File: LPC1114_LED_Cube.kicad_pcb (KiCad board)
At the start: 2 copper layers, 100 x 100 mm, 66 parts, among them Q201 BSS138, Q202 BSS138, Q203 BSS138, Q204 BSS138, Q205 IRLML6402TRPBF, Q206 IRLML6402TRPBF, Q207 IRLML6402TRPBF, Q208 IRLML6402TRPBF, Q209 BSS138, Q210 BSS138, Q211 BSS138, Q212 BSS138, Q213 IRLML6402TRPBF, Q214 IRLML6402TRPBF, Q215 IRLML6402TRPBF, Q216 IRLML6402TRPBF, Y101 12MHZ, Y102 12MHZ

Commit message: More pcb layout
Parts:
- moved LED/SPI_0 58.1 mm to (163.4, 83.1), turned to 0 degrees
- moved LED_CH0_CTRL0 0.50 mm to (92.7, 86.4)
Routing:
- net VPRG: track 0.00 -> 111.3 mm, vias 0 -> 5
- net XERR_CH0: track 0.00 -> 100.6 mm, vias 0 -> 4
- net DCPRG: track 0.00 -> 72.7 mm, vias 0 -> 4
- net ISP_ENTRY: track 0.00 -> 71.6 mm, vias 0 -> 4
- net XLAT: track 0.00 -> 61.8 mm, vias 0 -> 4
- net LED_DATA_SCK: track 0.00 -> 59.8 mm, vias 0 -> 4
- net BLANK: track 0.00 -> 59.6 mm, vias 0 -> 4
- net LED_CH2_8: track 0.00 -> 44.0 mm
- net LED_CH2_9: track 0.00 -> 40.4 mm
- net LED_CH3_0: track 0.00 -> 37.6 mm
- net LED_CH3_1: track 0.00 -> 37.3 mm, vias 0 -> 1
- net LED_CH3_2: track 0.00 -> 36.9 mm, vias 0 -> 1
- net LED_CH2_10: track 0.00 -> 36.7 mm
- net LED_CH3_3: track 0.00 -> 36.2 mm, vias 0 -> 1
- net LED_CH3_4: track 0.00 -> 34.5 mm, vias 0 -> 1
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
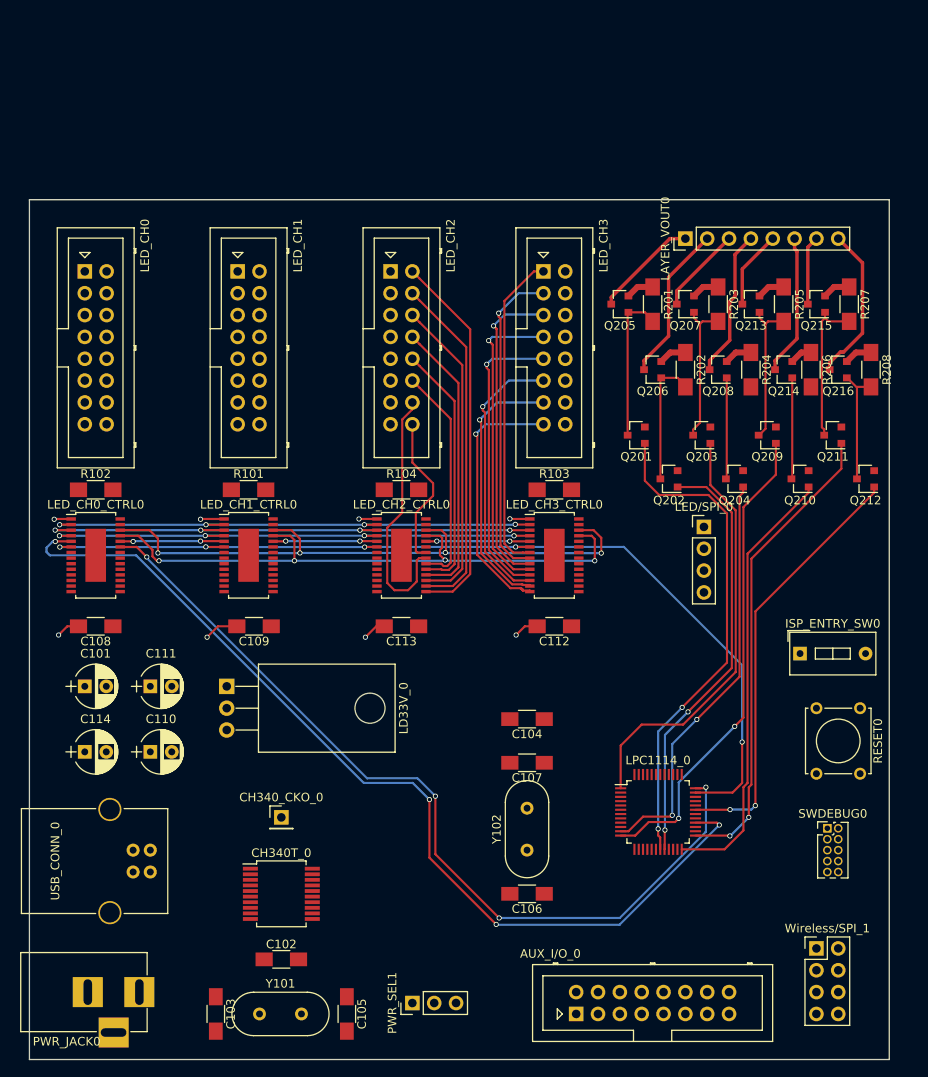
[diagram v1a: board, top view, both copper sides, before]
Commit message: redo layout for EMC
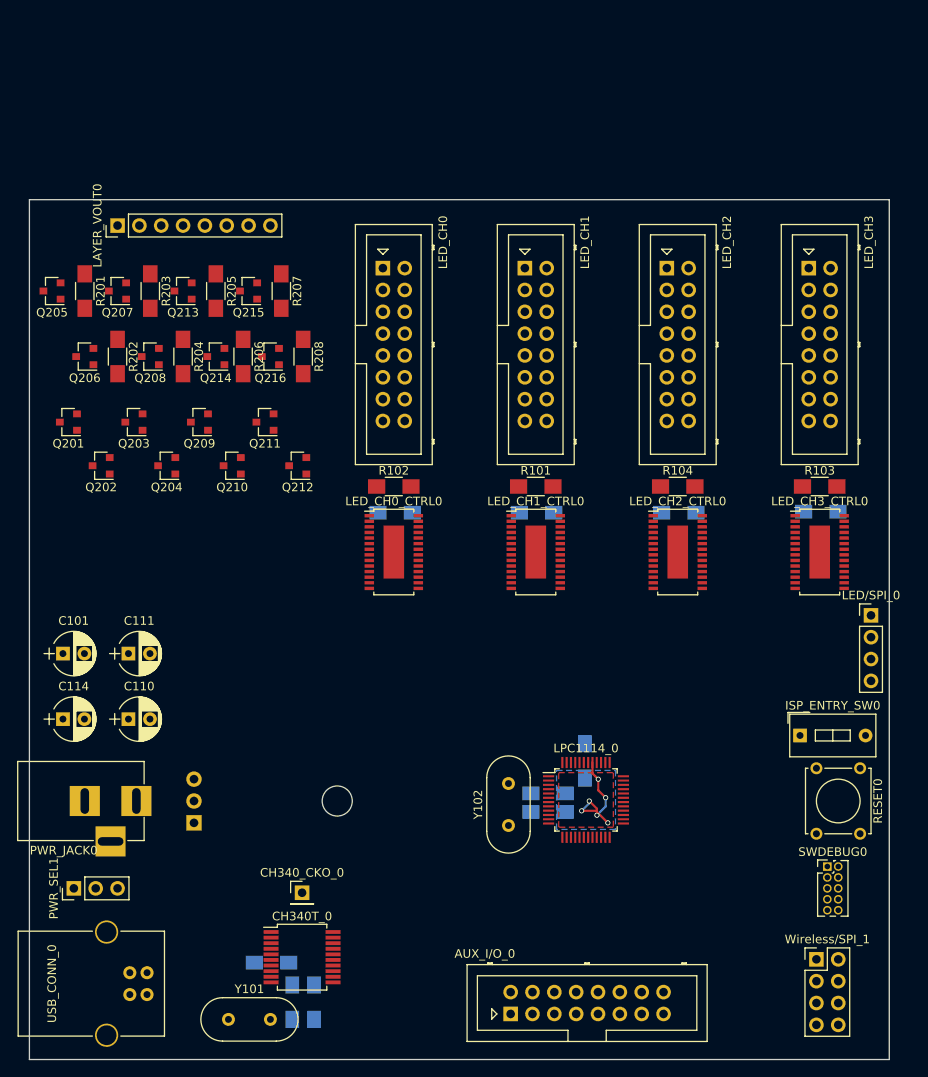
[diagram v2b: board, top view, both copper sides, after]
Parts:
- C102, C103, C104, C105, C106, C107, C108, C109, C112, C113, LD33V_0: moved to B.Cu
- moved Q210 66.1 mm to (108.6, 75.9)
- moved Q211 66.1 mm to (112.4, 70.9)
- moved Q212 66.1 mm to (116.2, 75.9)
- moved Q215 66.1 mm to (110.5, 55.6)
- moved R206 66.1 mm to (109.9, 63.2)
- moved R207 66.1 mm to (114.3, 55.6)
- moved LAYER_VOUT0 66.1 mm to (95.2, 48.0)
- moved Q201 66.1 mm to (89.5, 70.9)
- moved Q202 66.1 mm to (93.3, 75.9)
- moved Q203 66.1 mm to (97.2, 70.9)
- moved Q204 66.1 mm to (101.0, 75.9)
- moved Q205 66.1 mm to (87.6, 55.6)
- moved Q206 66.1 mm to (91.4, 63.2)
- moved Q207 66.1 mm to (95.2, 55.6)
- moved Q208 66.1 mm to (99.1, 63.2)
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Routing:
- net LED_SIN: track 111.5 -> 0.00 mm, vias 4 -> 0
- net VPRG: track 111.3 -> 0.00 mm, vias 5 -> 0
- net XERR_CH0: track 100.6 -> 0.00 mm, vias 4 -> 0
- net DCPRG: track 72.7 -> 0.00 mm, vias 4 -> 0
- net ISP_ENTRY: track 71.6 -> 0.00 mm, vias 4 -> 0
- net XLAT: track 61.8 -> 0.00 mm, vias 4 -> 0
- net LED_DATA_SCK: track 59.8 -> 0.00 mm, vias 4 -> 0
- net BLANK: track 59.6 -> 0.00 mm, vias 4 -> 0
- net LAYER_0_ON: track 57.9 -> 0.00 mm, vias 2 -> 0
- net LAYER_4_ON: track 55.9 -> 0.00 mm, vias 2 -> 0
- net LAYER_6_ON: track 55.1 -> 0.00 mm, vias 2 -> 0
- net LAYER_5_ON: track 51.2 -> 0.00 mm
- net LAYER_1_ON: track 49.9 -> 0.00 mm, vias 2 -> 0
- net LAYER_7_ON: track 49.9 -> 0.00 mm, vias 2 -> 0
- net LAYER_2_ON: track 49.7 -> 0.00 mm
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- added copper zone on B.Cu, net GND
- added copper zone on F.Cu, net GND
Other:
- rule trace_min: 0.2 -> 0.1524

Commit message: Fixed some schematic bugs. Added input mode switch.
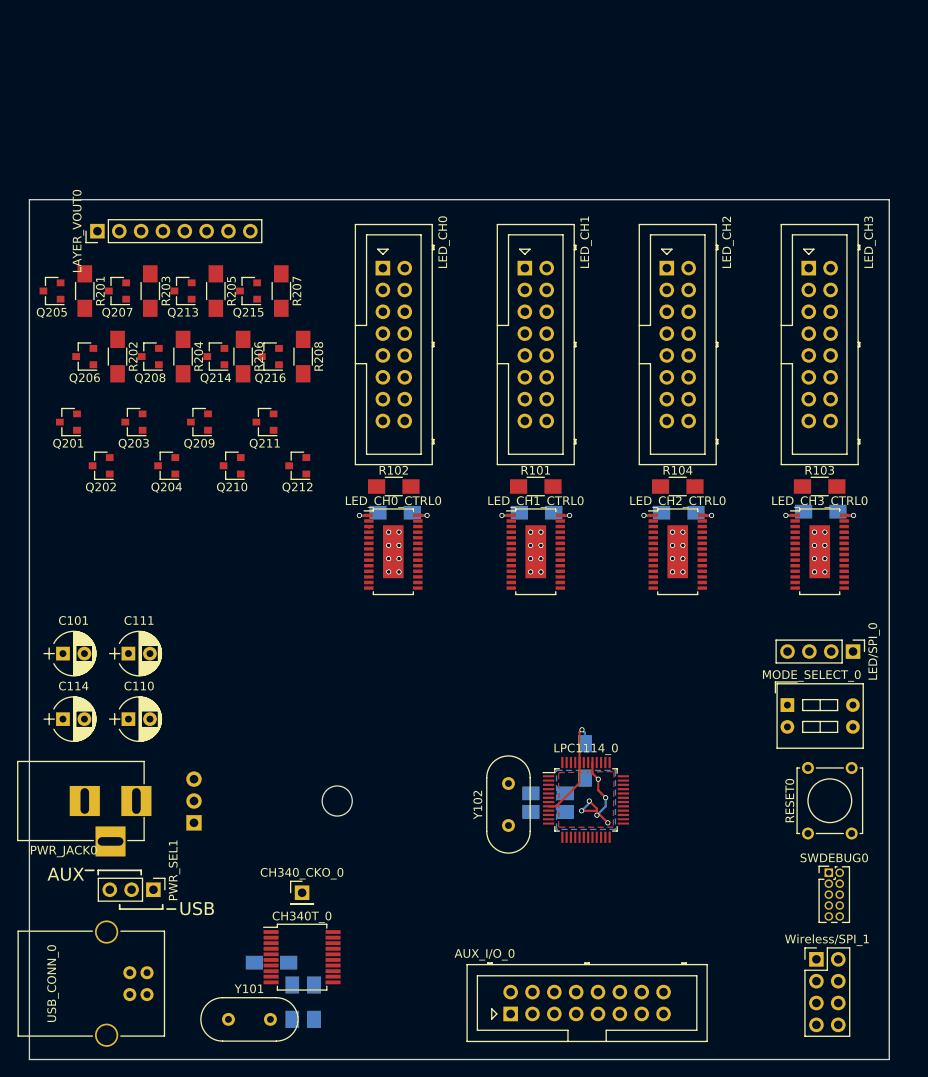
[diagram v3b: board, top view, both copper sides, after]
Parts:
- removed ISP_ENTRY_SW0: SW_DIP_x01, Buttons_Switches_THT:SW_DIP_x1_W7.62mm_Slide
- added MODE_SELECT_0: SW_DIP_x02, Buttons_Switches_THT:SW_DIP_x2_W7.62mm_Slide, F.Cu at (173.2, 103.8)
- moved RESET0 9.71 mm to (175.5, 118.7), turned to 90 degrees
- moved PWR_SEL1 9.26 mm to (99.4, 125.3), turned to 270 degrees
- moved LED/SPI_0 4.70 mm to (180.8, 97.6), turned to 270 degrees
- moved LAYER_VOUT0 2.43 mm to (92.9, 48.7)
- moved SWDEBUG0 0.75 mm to (178.0, 123.3)
- moved LED_CH0_CTRL0 0.07 mm to (127.3, 85.9)
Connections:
- net PIO0_2 renamed INPUT_MODE_SELECT
- C104 pad 1: +3V3 -> V3
- C108 pad 1: +3V3 -> V3
- C109 pad 1: +3V3 -> V3
- C112 pad 1: +3V3 -> V3
- C113 pad 1: +3V3 -> V3
- CH340T_0 pad 11: Net-(CH340T_0-Pad11) -> (no net)
- CH340T_0 pad 12: Net-(CH340T_0-Pad12) -> (no net)
- CH340T_0 pad 13: Net-(CH340T_0-Pad13) -> (no net)
- CH340T_0 pad 14: Net-(CH340T_0-Pad14) -> (no net)
- CH340T_0 pad 15: Net-(CH340T_0-Pad15) -> (no net)
- CH340T_0 pad 16: Net-(CH340T_0-Pad16) -> (no net)
- CH340T_0 pad 17: Net-(CH340T_0-Pad17) -> (no net)
- CH340T_0 pad 18: Net-(CH340T_0-Pad18) -> (no net)
- CH340T_0 pad 2: Net-(CH340T_0-Pad2) -> (no net)
- CH340T_0 pad 20: Net-(CH340T_0-Pad20) -> (no net)
- LED_CH0_CTRL0 pad 28: +3V3 -> V3
- LED_CH1_CTRL0 pad 28: +3V3 -> V3
- LED_CH2_CTRL0 pad 28: +3V3 -> V3
- LED_CH3_CTRL0 pad 28: +3V3 -> V3
- LPC1114_0 pad 44: +3V3 -> V3
- LPC1114_0 pad 8: +3V3 -> V3
- PWR_JACK0 pad 3: Net-(PWR_JACK0-Pad3) -> (no net)
- SWDEBUG0 pad 6: Net-(SWDEBUG0-Pad6) -> (no net)
- SWDEBUG0 pad 7: Net-(SWDEBUG0-Pad7) -> (no net)
- SWDEBUG0 pad 8: Net-(SWDEBUG0-Pad8) -> (no net)
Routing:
- net V3: track 0.00 -> 24.9 mm, vias 0 -> 5
- net GND: track 14.3 -> 28.8 mm, vias 6 -> 42
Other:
- board text added: "AUX"
- board text added: "USB"

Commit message: improved initial layout for better EMC and compactness Upgraded to KiCad 5.0
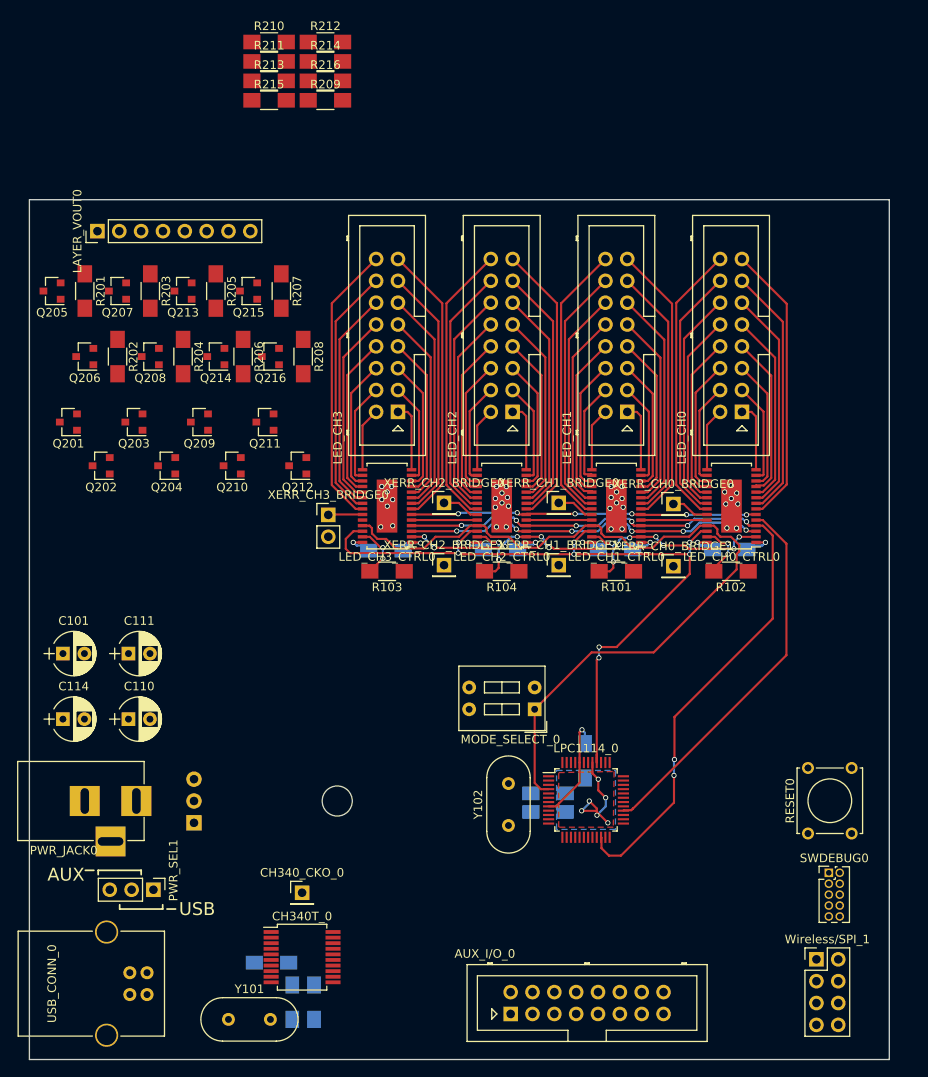
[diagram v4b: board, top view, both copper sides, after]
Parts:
- removed LED/SPI_0: Conn_01x04, Pin_Headers:Pin_Header_Straight_1x04_Pitch2.54mm
- added R209: 1K, Resistors_SMD:R_1206_HandSoldering, F.Cu at (119.4, 33.4)
- added R210: 1K, Resistors_SMD:R_1206_HandSoldering, F.Cu at (112.9, 26.7)
- added R211: 1K, Resistors_SMD:R_1206_HandSoldering, F.Cu at (112.9, 28.9)
- added R212: 1K, Resistors_SMD:R_1206_HandSoldering, F.Cu at (119.4, 26.7)
- added R213: 1K, Resistors_SMD:R_1206_HandSoldering, F.Cu at (112.9, 31.2)
- added R214: 1K, Resistors_SMD:R_1206_HandSoldering, F.Cu at (119.4, 28.9)
- added R215: 1K, Resistors_SMD:R_1206_HandSoldering, F.Cu at (112.9, 33.4)
- added R216: 1K, Resistors_SMD:R_1206_HandSoldering, F.Cu at (119.4, 31.2)
- added XERR_CH0_BRIDGE0: Conn_01x01, Pin_Headers:Pin_Header_Straight_1x01_Pitch2.54mm, F.Cu at (159.9, 80.4)
- added XERR_CH0_BRIDGE1: Conn_01x01, Pin_Headers:Pin_Header_Straight_1x01_Pitch2.54mm, F.Cu at (159.9, 87.6)
- added XERR_CH1_BRIDGE0: Conn_01x01, Pin_Headers:Pin_Header_Straight_1x01_Pitch2.54mm, F.Cu at (146.6, 80.3)
- added XERR_CH1_BRIDGE1: Conn_01x01, Pin_Headers:Pin_Header_Straight_1x01_Pitch2.54mm, F.Cu at (146.6, 87.5)
- added XERR_CH2_BRIDGE0: Conn_01x01, Pin_Headers:Pin_Header_Straight_1x01_Pitch2.54mm, F.Cu at (133.2, 80.3)
- added XERR_CH2_BRIDGE1: Conn_01x01, Pin_Headers:Pin_Header_Straight_1x01_Pitch2.54mm, F.Cu at (133.2, 87.5)
- added XERR_CH3_BRIDGE0: Conn_01x02, Pin_Headers:Pin_Header_Straight_1x02_Pitch2.54mm, F.Cu at (119.8, 81.7)
- moved R103 51.3 mm to (126.6, 88.2), turned to 180 degrees
- moved C112 50.8 mm to (126.5, 85.8), turned to 0 degrees
- moved LED_CH3 50.6 mm to (127.9, 69.7), turned to 90 degrees
- moved LED_CH3_CTRL0 50.6 mm to (126.6, 80.6), turned to 180 degrees
- moved LED_CH0 45.0 mm to (167.9, 69.7), turned to 90 degrees
- moved R102 40.4 mm to (166.6, 88.2), turned to 180 degrees
- moved LED_CH0_CTRL0 39.7 mm to (166.7, 80.6), turned to 180 degrees
- moved C108 39.1 mm to (166.4, 85.7), turned to 0 degrees
- moved MODE_SELECT_0 29.4 mm to (143.8, 104.3), turned to 180 degrees
- moved LED_CH2 24.5 mm to (141.2, 69.7), turned to 90 degrees
- moved R104 22.7 mm to (139.9, 88.2), turned to 180 degrees
- moved C113 21.2 mm to (139.8, 85.7), turned to 0 degrees
- moved LED_CH2_CTRL0 21.1 mm to (139.9, 80.6), turned to 180 degrees
- moved LED_CH1 20.5 mm to (154.5, 69.7), turned to 90 degrees
- moved R101 13.6 mm to (153.3, 88.2), turned to 180 degrees
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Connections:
- CH340T_0 pad 11: (no net) -> Net-(CH340T_0-Pad11)
- CH340T_0 pad 12: (no net) -> Net-(CH340T_0-Pad12)
- CH340T_0 pad 13: (no net) -> Net-(CH340T_0-Pad13)
- CH340T_0 pad 14: (no net) -> Net-(CH340T_0-Pad14)
- CH340T_0 pad 15: (no net) -> Net-(CH340T_0-Pad15)
- CH340T_0 pad 16: (no net) -> Net-(CH340T_0-Pad16)
- CH340T_0 pad 17: (no net) -> Net-(CH340T_0-Pad17)
- CH340T_0 pad 18: (no net) -> Net-(CH340T_0-Pad18)
- CH340T_0 pad 2: (no net) -> Net-(CH340T_0-Pad2)
- CH340T_0 pad 20: (no net) -> Net-(CH340T_0-Pad20)
- LED_CH0 pad 1: LED_CH0_0 -> LED_CH0_7
- LED_CH0 pad 11: LED_CH0_5 -> LED_CH0_2
- LED_CH0 pad 13: LED_CH0_6 -> LED_CH0_1
- LED_CH0 pad 15: LED_CH0_7 -> LED_CH0_0
- LED_CH0 pad 3: LED_CH0_1 -> LED_CH0_6
- LED_CH0 pad 5: LED_CH0_2 -> LED_CH0_5
- LED_CH0 pad 7: LED_CH0_3 -> LED_CH0_4
- LED_CH0 pad 9: LED_CH0_4 -> LED_CH0_3
- LED_CH1 pad 1: LED_CH1_0 -> LED_CH1_7
- LED_CH1 pad 11: LED_CH1_5 -> LED_CH1_2
- LED_CH1 pad 13: LED_CH1_6 -> LED_CH1_1
- LED_CH1 pad 15: LED_CH1_7 -> LED_CH1_0
- LED_CH1 pad 3: LED_CH1_1 -> LED_CH1_6
- LED_CH1 pad 5: LED_CH1_2 -> LED_CH1_5
- LED_CH1 pad 7: LED_CH1_3 -> LED_CH1_4
- LED_CH1 pad 9: LED_CH1_4 -> LED_CH1_3
- LED_CH2 pad 1: LED_CH2_0 -> LED_CH2_7
- LED_CH2 pad 11: LED_CH2_5 -> LED_CH2_2
- LED_CH2 pad 13: LED_CH2_6 -> LED_CH2_1
- LED_CH2 pad 15: LED_CH2_7 -> LED_CH2_0
- LED_CH2 pad 3: LED_CH2_1 -> LED_CH2_6
- LED_CH2 pad 5: LED_CH2_2 -> LED_CH2_5
- LED_CH2 pad 7: LED_CH2_3 -> LED_CH2_4
- LED_CH2 pad 9: LED_CH2_4 -> LED_CH2_3
- LED_CH3 pad 1: LED_CH3_0 -> LED_CH3_7
- LED_CH3 pad 11: LED_CH3_5 -> LED_CH3_2
- LED_CH3 pad 13: LED_CH3_6 -> LED_CH3_1
- LED_CH3 pad 15: LED_CH3_7 -> LED_CH3_0
- LED_CH3 pad 3: LED_CH3_1 -> LED_CH3_6
- LED_CH3 pad 5: LED_CH3_2 -> LED_CH3_5
- LED_CH3 pad 7: LED_CH3_3 -> LED_CH3_4
- LED_CH3 pad 9: LED_CH3_4 -> LED_CH3_3
- LPC1114_0 pad 36: XERR_CH0 -> XERR_MCU_CH0
- LPC1114_0 pad 37: XERR_CH1 -> XERR_MCU_CH1
- LPC1114_0 pad 43: XERR_CH2 -> XERR_MCU_CH2
- LPC1114_0 pad 48: XERR_CH3 -> XERR_MCU_CH3
- PWR_JACK0 pad 3: (no net) -> Net-(PWR_JACK0-Pad3)
- SWDEBUG0 pad 6: (no net) -> Net-(SWDEBUG0-Pad6)
- SWDEBUG0 pad 7: (no net) -> Net-(SWDEBUG0-Pad7)
- SWDEBUG0 pad 8: (no net) -> Net-(SWDEBUG0-Pad8)
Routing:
- net ISP_ENTRY: track 0.00 -> 98.4 mm
- net LED_DATA_SCK: track 0.00 -> 94.0 mm, vias 0 -> 8
- net DCPRG: track 0.00 -> 86.6 mm, vias 0 -> 8
- net BLANK: track 0.00 -> 45.2 mm, vias 0 -> 12
- net LED_SIN: track 0.00 -> 44.1 mm
- net XLAT: track 0.12 -> 42.7 mm, vias 0 -> 6
- net VPRG: track 0.00 -> 40.3 mm, vias 0 -> 6
- net LED_CH1_0: track 0.00 -> 33.2 mm
- net LED_CH3_15: track 0.00 -> 33.1 mm
- net LED_CH2_15: track 0.00 -> 33.1 mm
- net LED_CH1_15: track 0.00 -> 33.1 mm
- net LED_CH0_0: track 0.00 -> 33.1 mm
- net LED_CH3_0: track 0.00 -> 33.1 mm
- net LED_CH0_15: track 0.00 -> 33.1 mm
- net LED_CH2_0: track 0.00 -> 33.1 mm
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
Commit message: more layout
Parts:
- moved R210 57.9 mm to (95.2, 81.8), turned to 90 degrees
- moved R212 57.6 mm to (103.0, 81.9), turned to 90 degrees
- moved R214 53.7 mm to (110.5, 81.9), turned to 90 degrees
- moved R216 50.7 mm to (118.0, 81.9), turned to 90 degrees
- moved R209 47.2 mm to (93.5, 72.9), turned to 90 degrees
- moved R211 45.5 mm to (101.2, 72.9), turned to 90 degrees
- moved R213 42.0 mm to (108.7, 72.9), turned to 90 degrees
- moved R215 40.3 mm to (116.3, 73.6), turned to 90 degrees
- moved XERR_CH3_BRIDGE0 6.90 mm to (121.3, 88.4)
- moved Q202 4.44 mm to (92.3, 80.3)
- moved Q204 4.44 mm to (99.9, 80.3)
- moved Q212 4.44 mm to (115.2, 80.3)
- moved Q210 4.44 mm to (107.6, 80.3)
- moved Q216 4.09 mm to (114.8, 66.9)
- moved R208 4.09 mm to (118.6, 66.9)
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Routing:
- net V5: track 0.00 -> 78.1 mm, vias 0 -> 11
- net GND: track 28.8 -> 65.8 mm, vias 46 -> 54
- net /LayerController/LAYER_7_PWR: track 0.00 -> 19.1 mm
- net Net-(Q211-Pad3): track 0.00 -> 17.7 mm
- net Net-(Q203-Pad3): track 0.00 -> 17.7 mm
- net Net-(Q209-Pad3): track 0.00 -> 17.7 mm
- net Net-(Q201-Pad3): track 0.00 -> 17.6 mm
- net Net-(Q212-Pad3): track 0.00 -> 17.5 mm
- net /LayerController/LAYER_5_PWR: track 0.00 -> 16.9 mm
- net Net-(Q202-Pad3): track 0.00 -> 16.7 mm
- net Net-(Q204-Pad3): track 0.00 -> 16.7 mm
- net /LayerController/LAYER_1_PWR: track 0.00 -> 16.7 mm
- net Net-(Q210-Pad3): track 0.00 -> 15.8 mm
- net /LayerController/LAYER_3_PWR: track 0.00 -> 15.7 mm
- net /LayerController/LAYER_0_PWR: track 0.00 -> 10.3 mm
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
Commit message: more PCB layout
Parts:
- moved MODE_SELECT_0 16.6 mm to (158.0, 95.8)
- moved C107 16.4 mm to (158.1, 103.7)
- moved LPC1114_0 16.4 mm to (162.5, 104.4)
- moved C104 16.4 mm to (162.4, 99.9)
- moved C106 16.4 mm to (158.1, 105.8)
- moved Y102 16.4 mm to (153.5, 107.4)
- moved XERR_CH1_BRIDGE1 2.87 mm to (149.4, 88.2)
- moved XERR_CH2_BRIDGE1 2.87 mm to (136.0, 88.2)
- moved XERR_CH0_BRIDGE1 2.85 mm to (162.7, 88.2)
- moved C109 2.79 mm to (156.0, 85.7)
- moved C113 2.79 mm to (142.6, 85.7)
- moved LED_CH1 2.79 mm to (157.3, 69.7)
- moved LED_CH1_CTRL0 2.79 mm to (156.1, 80.6)
- moved LED_CH2 2.79 mm to (144.0, 69.7)
- moved LED_CH3_CTRL0 2.79 mm to (129.4, 80.6)
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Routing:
- net V3: track 25.0 -> 204.6 mm, vias 5 -> 10
- net LAYER_0_ON: track 2.04 -> 98.7 mm, vias 0 -> 2
- net LAYER_6_ON: track 1.82 -> 89.9 mm, vias 0 -> 2
- net LAYER_1_ON: track 4.05 -> 87.0 mm, vias 0 -> 2
- net LAYER_4_ON: track 2.03 -> 79.0 mm, vias 0 -> 2
- net LAYER_2_ON: track 2.16 -> 78.7 mm, vias 0 -> 4
- net LAYER_5_ON: track 3.50 -> 79.1 mm, vias 0 -> 2
- net LAYER_7_ON: track 3.41 -> 76.8 mm, vias 0 -> 2
- net LAYER_3_ON: track 3.52 -> 71.5 mm, vias 0 -> 2
- net PIO0_7: track 0.00 -> 35.7 mm, vias 0 -> 2
- net DCPRG: track 86.6 -> 56.7 mm, vias 8 -> 6
- net LED_DATA_SCK: track 94.0 -> 81.5 mm
- net LED_SIN: track 44.1 -> 32.2 mm
- net ISP_ENTRY: track 98.4 -> 88.8 mm
- net Net-(C106-Pad1): track 0.00 -> 9.05 mm
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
